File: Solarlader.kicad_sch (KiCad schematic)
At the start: 38 parts, among them J3 UKDBBTAAA, Q1 HJ8205, Q2 AO3400A, U1 LGS5600, U2 DW01A, U3 74AHC1G14GV,125

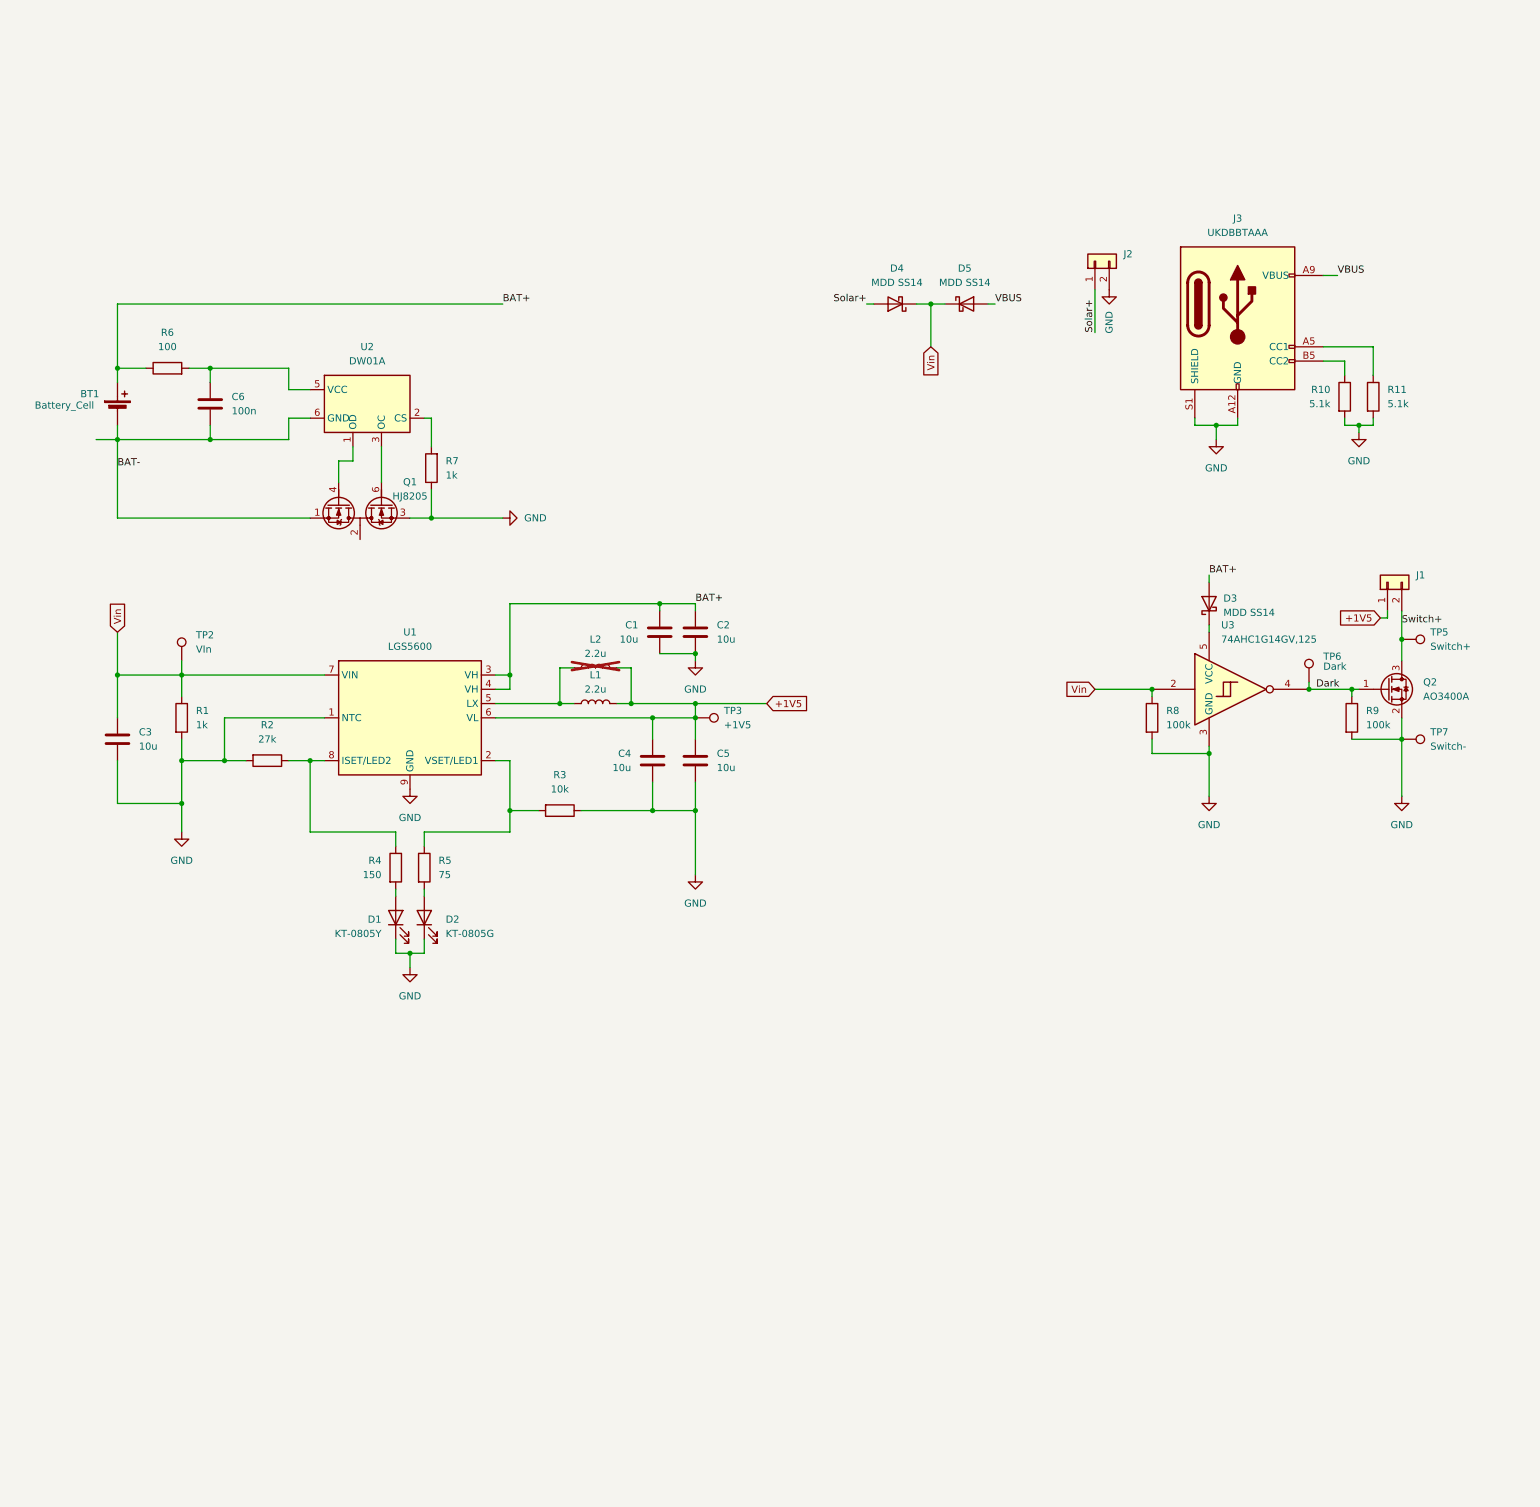
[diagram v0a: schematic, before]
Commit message: Stand mit 1.5V
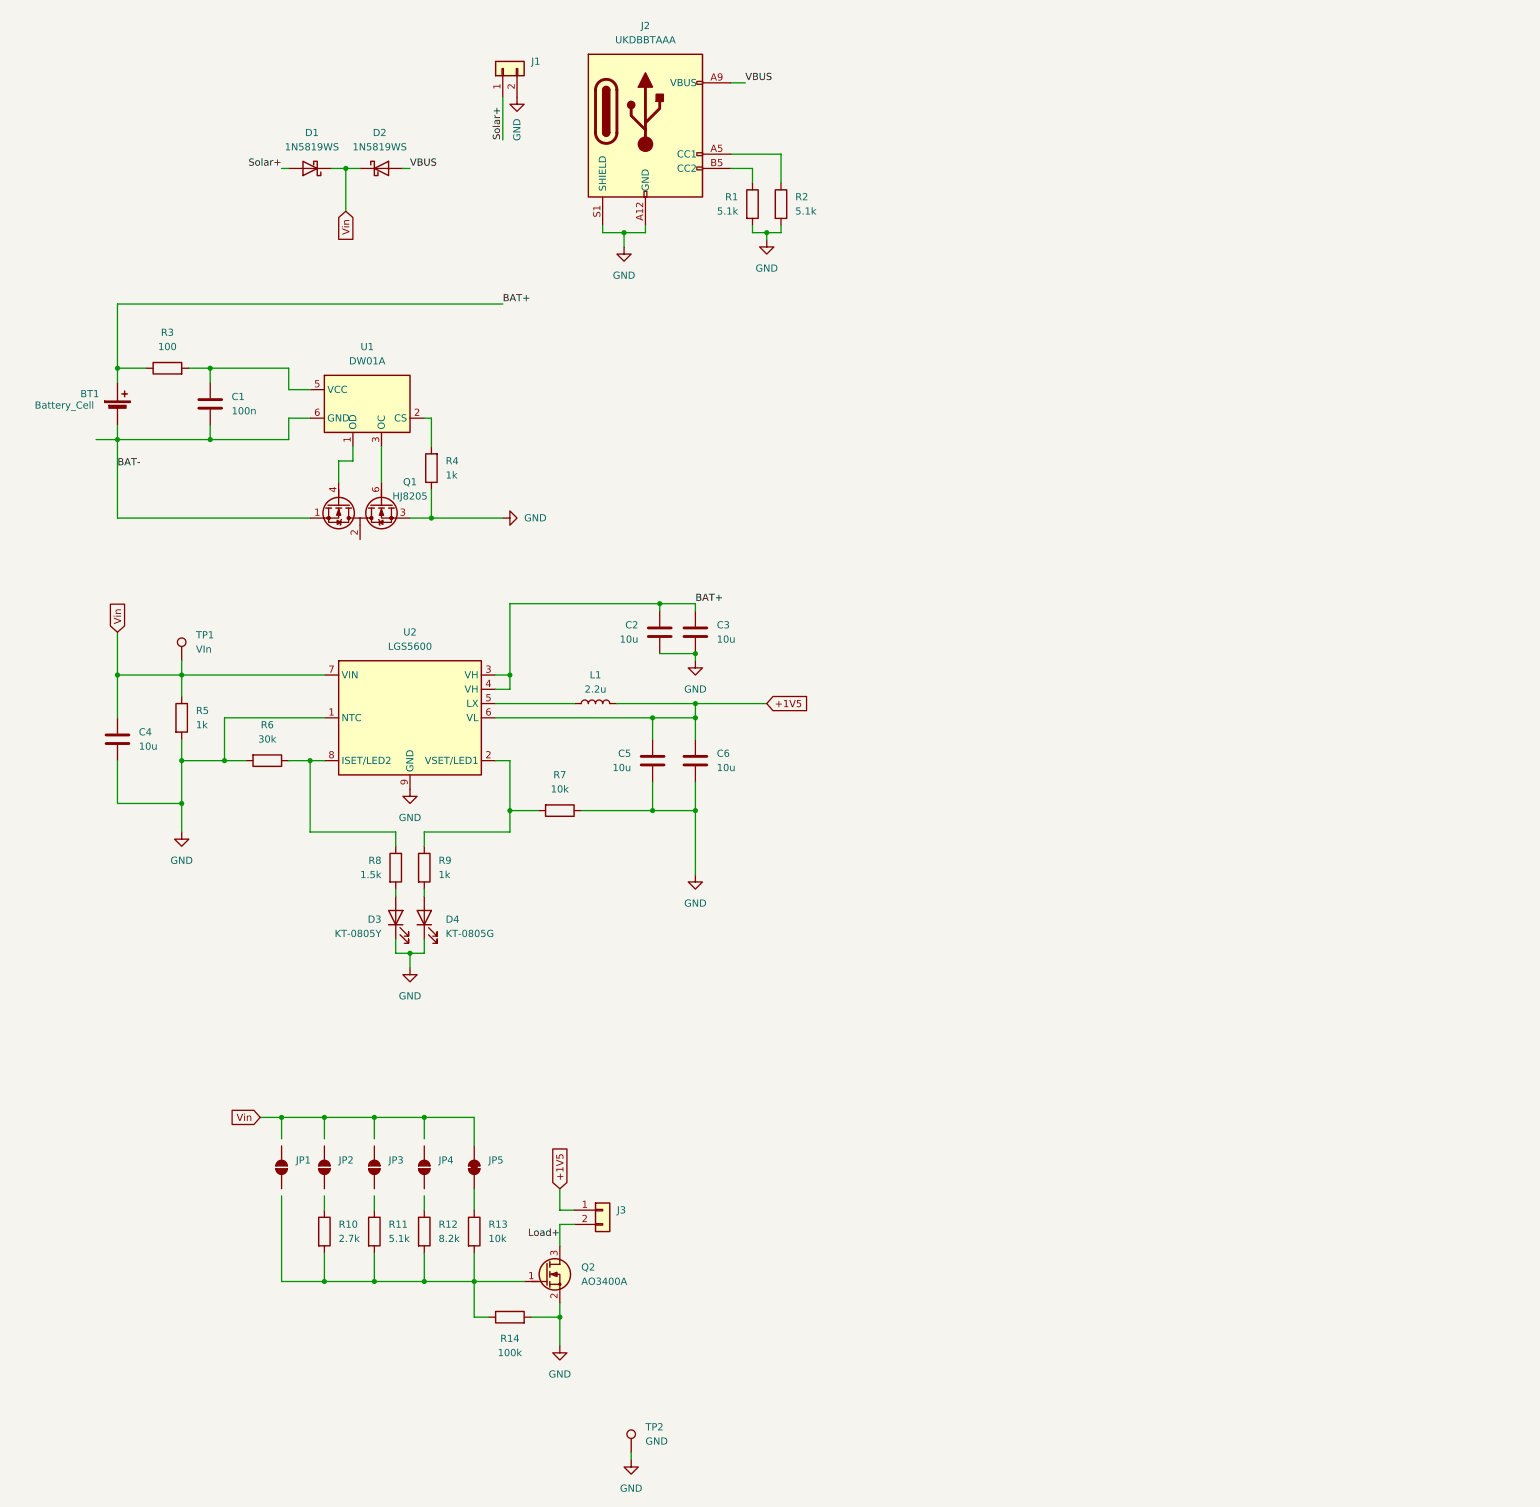
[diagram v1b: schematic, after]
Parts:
- removed D3: MDD SS14, Diode_SMD:D_SMA, symbol Device:D_Schottky
- removed L2: 2.2u, Inductor_SMD:L_APV_ANR4010, symbol Device:L
- removed Q2: AO3400A, Package_TO_SOT_SMD:SOT-23, symbol Transistor_FET:Q_NMOS_GSD
- removed R8, R9: 100k, Resistor_SMD:R_0402_1005Metric, symbol Device:R
- removed TP3: +1V5, TestPoint:TestPoint_Pad_D1.0mm, symbol Connector:TestPoint
- removed TP5: Switch+, TestPoint:TestPoint_Pad_D1.0mm, symbol Connector:TestPoint
- removed TP6: Dark, TestPoint:TestPoint_Pad_D1.0mm, symbol Connector:TestPoint
- removed U3: 74AHC1G14GV,125, Package_SO:TSOP-5_1.65x3.05mm_P0.95mm, symbol 74xGxx:74AHC1G14
- added JP1, JP2, JP3, JP4: SolderJumper_2_Open, Jumper:SolderJumper-2_P1.3mm_Open_Pad1.0x1.5mm, symbol Jumper:SolderJumper_2_Open
- added JP5: SolderJumper_2_Bridged, Jumper:SolderJumper-2_P1.3mm_Bridged2Bar_Pad1.0x1.5mm, symbol Jumper:SolderJumper_2_Bridged
- added Q2: AO3400A, PCM_Package_TO_SOT_SMD_AKL:SOT-23, symbol PCM_Transistor_MOSFET_AKL:AO3400A
- added R10: 2.7k, Resistor_SMD:R_0402_1005Metric, symbol Device:R
- added R11: 5.1k, Resistor_SMD:R_0402_1005Metric, symbol Device:R
- added R12: 8.2k, Resistor_SMD:R_0603_1608Metric, symbol Device:R
- added R13: 10k, Resistor_SMD:R_0402_1005Metric, symbol Device:R
- added R14: 100k, Resistor_SMD:R_0402_1005Metric, symbol Device:R
- C1: renamed from C6; footprint Capacitor_SMD:C_0402_1005Metric -> Capacitor_SMD:C_0805_2012Metric
- D1: renamed from D4; value MDD SS14 -> 1N5819WS; footprint Diode_SMD:D_SMA -> Diode_SMD:D_SOD-323_HandSoldering
- D2: renamed from D5; value MDD SS14 -> 1N5819WS; footprint Diode_SMD:D_SMA -> Diode_SMD:D_SOD-323_HandSoldering
- R3: renamed from R6; footprint Resistor_SMD:R_0402_1005Metric -> Resistor_SMD:R_0805_2012Metric
- R6: renamed from R2; value 27k -> 30k; footprint Resistor_SMD:R_0402_1005Metric -> Resistor_SMD:R_0603_1608Metric
- R8: renamed from R4; value 150 -> 1.5k; footprint Resistor_SMD:R_0402_1005Metric -> Resistor_SMD:R_0603_1608Metric
- R9: renamed from R5; value 75 -> 1k; footprint Resistor_SMD:R_0402_1005Metric -> Resistor_SMD:R_0603_1608Metric
- TP1: renamed from TP2; footprint TestPoint:TestPoint_Pad_D2.0mm -> TestPoint:TestPoint_Pad_D1.0mm
- TP2: renamed from TP7; value Switch- -> GND; footprint TestPoint:TestPoint_Pad_D2.0mm -> TestPoint:TestPoint_Pad_D1.0mm
- renumbered C1 to C2, C2 to C3, C3 to C4, C4 to C5, C5 to C6, D1 to D3, D2 to D4, J2 to J1, J3 to J2, J1 to J3, R10 to R1, R11 to R2, R7 to R4, R1 to R5, R3 to R7, U2 to U1, U1 to U2
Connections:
- net GND: now also Q2.2 (S), R14.2
- net Vin: now also JP5.2 (B)
- net Switch+ renamed Load+
- net Load+: now also Q2.3 (D)
- new net: Q2.1 (G), R10.2, R11.2, R12.2, R13.2, R14.1
- new net: JP5.1 (A), R13.1
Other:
- moved on the sheet: D1, D2, J1, J2, J3, R1, R2, TP2

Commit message: V2
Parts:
- removed C6: 10u, Capacitor_SMD:C_0402_1005Metric, symbol Device:C
- removed JP1, JP2, JP3, JP4: SolderJumper_2_Open, Jumper:SolderJumper-2_P1.3mm_Open_Pad1.0x1.5mm, symbol Jumper:SolderJumper_2_Open
- removed JP5: SolderJumper_2_Bridged, Jumper:SolderJumper-2_P1.3mm_Bridged2Bar_Pad1.0x1.5mm, symbol Jumper:SolderJumper_2_Bridged
- removed R11: 5.1k, Resistor_SMD:R_0402_1005Metric, symbol Device:R
- removed R8: 1.5k, Resistor_SMD:R_0603_1608Metric, symbol Device:R
- removed R9: 1k, Resistor_SMD:R_0603_1608Metric, symbol Device:R
- removed TP1: VIn, TestPoint:TestPoint_Pad_D1.0mm, symbol Connector:TestPoint
- removed U2: LGS5600, Package_DFN_QFN:DFN-8-1EP_2x2mm_P0.5mm_EP0.9x1.6mm, symbol battery_holder:LGS5600
- added C1, C10: 100u, Capacitor_Tantalum_SMD:CP_EIA-3528-21_Kemet-B, symbol Device:C_Polarized
- added C7: 10u, Capacitor_SMD:C_0603_1608Metric, symbol Device:C
- added C8: 10u, Capacitor_SMD:C_0402_1005Metric, symbol Device:C
- added C9: 20u, Capacitor_SMD:C_1206_3216Metric, symbol Device:C
- added D3: DSL34, Diode_SMD:D_SOD-123F, symbol Device:D_Schottky
- added L2: 2.2u, Inductor_SMD:L_APV_ANR4020, symbol Device:L
- added R13, R4: 680k, Resistor_SMD:R_0603_1608Metric, symbol Device:R
- added R14: 2k, Resistor_SMD:R_0402_1005Metric, symbol Device:R
- added R15: 100k, Resistor_SMD:R_0402_1005Metric, symbol Device:R
- added R3: 51k, Resistor_SMD:R_0402_1005Metric, symbol Device:R
- added U1, U4: TPS61022, Package_DFN_QFN:Texas_RWU0007A_VQFN-7_2x2mm_P0.5mm, symbol Converter_DCDC:TPS61022
- added U2: TP4057, Package_TO_SOT_SMD:TSOT-23-6, symbol Battery_Management:TP4057
- BT1: footprint Connector_Wire:SolderWire-0.5sqmm_1x02_P4.6mm_D0.9mm_OD2.1mm -> Connector_JST:JST_PH_S2B-PH-K_1x02_P2.00mm_Horizontal; symbol Device:Battery_Cell -> Connector:Conn_01x02_Pin; now in the parts list
- C2, C4: footprint Capacitor_SMD:C_0402_1005Metric -> Capacitor_SMD:C_0603_1608Metric
- C3: value 10u -> 20u; footprint Capacitor_SMD:C_0402_1005Metric -> Capacitor_SMD:C_1206_3216Metric; LCSC (none) -> C5672
- C5: value 10u -> 1u
- D1, D2: value 1N5819WS -> DSL34; footprint Diode_SMD:D_SOD-323_HandSoldering -> Diode_SMD:D_SOD-123F
- J1, J3: footprint Connector_Wire:SolderWire-0.25sqmm_1x02_P4.2mm_D0.65mm_OD1.7mm -> Connector_Wire:SolderWire-0.1sqmm_1x02_P3.6mm_D0.4mm_OD1mm
- L1: footprint Inductor_SMD:L_0805_2012Metric -> Inductor_SMD:L_APV_ANR4020; LCSC (none) -> C520302
- R10: value 2.7k -> 1.6k; footprint Resistor_SMD:R_0402_1005Metric -> Resistor_SMD:R_0603_1608Metric
- R12: value 8.2k -> 51k; footprint Resistor_SMD:R_0603_1608Metric -> Resistor_SMD:R_0402_1005Metric
- R16: renamed from R13; value 10k -> 100
- R5: value 1k -> 2k
- R6: value 30k -> 100k; footprint Resistor_SMD:R_0603_1608Metric -> Resistor_SMD:R_0402_1005Metric
- R7: value 10k -> 1k; footprint Resistor_SMD:R_0402_1005Metric -> Resistor_SMD:R_0603_1608Metric
- renumbered C1 to C6, D3 to D4, D4 to D5, R4 to R11, R14 to R17, R3 to R9, TP2 to TP1, U1 to U3
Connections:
- net BAT-: now also BT1.2 (Pin_2), C10.2; no longer BT1.1 (-)
- net GND: now also R10.2, C1.2, C7.1, C8.2, C9.2, R15.2, U1.1 (GND), U1.6 (MODE), U2.2 (GND), U4.1 (GND), U4.6 (MODE); no longer D4.1 (K), D5.1 (K), R5.2, R7.1
- net at Q2.1 (G), R16.2, R17.1: no longer R10.2, R12.2
- net at R10.1: now also U2.6 (PROG)
- net at R6.1: now also R5.2, U1.4 (FB)
- net at R7.2: now also D4.2 (A), D5.2 (A)
- net VIN: now reaches L1.1
- net VIN: now also C2.1, D1.1 (K), D2.1 (K), C1.1, D3.2 (A), U1.5 (EN), U1.7 (VIN)
- net +4V5: now reaches R12.1
- net +4V5: now also C9.1, U4.3 (VOUT)
- removed net +1V5: C5.1, J3.1 (Pin_1), L1.2
- removed net BAT+: BT1.2 (+), C2.1, C3.1, R9.1
- removed net Vin: C4.1, D1.1 (K), D2.1 (K), R5.1
- new net: L2.2, U4.2 (SW)
- new net: R14.2, R15.1, U4.4 (FB)
- new net: L1.2, U1.2 (SW)
- new net: D5.1 (K), U2.1 (~{CHRG})
- new net: D4.1 (K), U2.5 (STDBY)
- new net: R4.2, R5.1
- new net: R13.2, R14.1
- new net: R12.2, R13.1
- new net: R3.2, R4.1
- new net +5V: C3.1, C4.1, C5.1, D3.1 (K), R3.1, R7.1, U1.3 (VOUT), U2.4 (V_{CC})
- new net +BATT: BT1.1 (Pin_1), C10.1, C7.2, C8.1, L2.1, R9.1, U2.3 (BAT), U4.5 (EN), U4.7 (VIN)
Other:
- moved on the sheet: BT1, C6, D2, D4, D5, J1, J2, J3, Q1, Q2, R1, R11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

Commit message: Saved between
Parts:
- removed C7: 10u, Capacitor_SMD:C_0603_1608Metric, symbol Device:C
- removed C8: 10u, Capacitor_SMD:C_0402_1005Metric, symbol Device:C
- removed C9: 20u, Capacitor_SMD:C_1206_3216Metric, symbol Device:C
- removed D3: DSL34, Diode_SMD:D_SOD-123F, symbol Device:D_Schottky
- removed D5: KT-0805G, LED_SMD:LED_0805_2012Metric, symbol Device:LED
- removed J3: ~, Connector_Wire:SolderWire-0.1sqmm_1x02_P3.6mm_D0.4mm_OD1mm, symbol Connector_Generic:Conn_01x02
- removed L1, L2: 2.2u, Inductor_SMD:L_APV_ANR4020, symbol Device:L
- removed Q2: AO3400A, PCM_Package_TO_SOT_SMD_AKL:SOT-23, symbol PCM_Transistor_MOSFET_AKL:AO3400A
- removed R10: 1.6k, Resistor_SMD:R_0603_1608Metric, symbol Device:R
- removed R12: 51k, Resistor_SMD:R_0402_1005Metric, symbol Device:R
- removed R13: 680k, Resistor_SMD:R_0603_1608Metric, symbol Device:R
- removed R14: 2k, Resistor_SMD:R_0402_1005Metric, symbol Device:R
- removed R15, R17: 100k, Resistor_SMD:R_0402_1005Metric, symbol Device:R
- removed R16: 100, Resistor_SMD:R_0402_1005Metric, symbol Device:R
- removed TP1: GND, TestPoint:TestPoint_Pad_D1.0mm, symbol Connector:TestPoint
- removed U1, U4: TPS61022, Package_DFN_QFN:Texas_RWU0007A_VQFN-7_2x2mm_P0.5mm, symbol Converter_DCDC:TPS61022
- removed U2: TP4057, Package_TO_SOT_SMD:TSOT-23-6, symbol Battery_Management:TP4057
- added D3: KT-0603W, LED_SMD:LED_0603_1608Metric, symbol Device:LED
- added H1, H2: MountingHole, MountingHole:MountingHole_2.2mm_M2_DIN965, symbol Mechanical:MountingHole
- added U1: BQ25185, Snapeda:WSON10_DLH_TEX-L, symbol battery_holder:BQ25185
- BT1: now not fitted
- C2: value 10u -> 2.2u 25V; footprint Capacitor_SMD:C_0603_1608Metric -> Capacitor_SMD:C_0805_2012Metric; now not fitted
- C3: value 20u -> 0.1u 25V; footprint Capacitor_SMD:C_1206_3216Metric -> Capacitor_SMD:C_0402_1005Metric; LCSC C5672 -> (none)
- C4: value 10u -> 1u 35V
- C5: value 1u -> 10p 10V
- D4: value KT-0805Y -> KT-0603Y2; footprint LED_SMD:LED_0805_2012Metric -> LED_SMD:LED_0603_1608Metric
- R3: value 51k -> 18k
- R4: value 680k -> 620
- R5: value 2k -> 10k
- R6: value 100k -> 510
- R7: value 1k -> 300; footprint Resistor_SMD:R_0603_1608Metric -> Resistor_SMD:R_0402_1005Metric
- U3: value DW01A -> DW01A - C686633
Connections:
- net +BATT: now also C4.1, U1.2 (BAT)
- net GND: now also R3.2, R4.2, R5.2, U1.11 (EPAD), U1.4 (~{CE}), U1.5 (GND); no longer R6.2
- net VIN: now also C3.1, U1.10 (IN)
- net at R7.2: now also D3.2 (A); no longer D4.2 (A)
- net VCC: now reaches C6.1, R9.2, U3.5 (VCC)
- net STAT2: now reaches D4.1 (K)
- net STAT2: now also U1.3 (STAT2)
- net TS/MR: now reaches R5.1
- net TS/MR: now also U1.6 (TS/MR); no longer R4.2
- net VSYS: now reaches R6.1
- net VSYS: now also C5.1, R7.1, U1.1 (SYS); no longer R5.2
- net CS: now reaches R11.2, U3.2 (CS)
- net ISET: now reaches R4.1
- net ISET: now also U1.8 (ISET); no longer R3.2
- removed net +5V: C3.1, C4.1, C5.1, R3.1, R7.1
- net BAT- renamed -BATT
- new net: D4.2 (A), R6.2
- new net ILIM: R3.1, U1.7 (ILIM/VSET)
- new net STAT1: D3.1 (K), U1.9 (STAT1)
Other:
- moved on the sheet: C10, C6, D1, D2, J1, J2, Q1, R1, R11, R2, R9, U3
